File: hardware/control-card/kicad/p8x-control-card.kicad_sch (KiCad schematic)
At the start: 0 parts

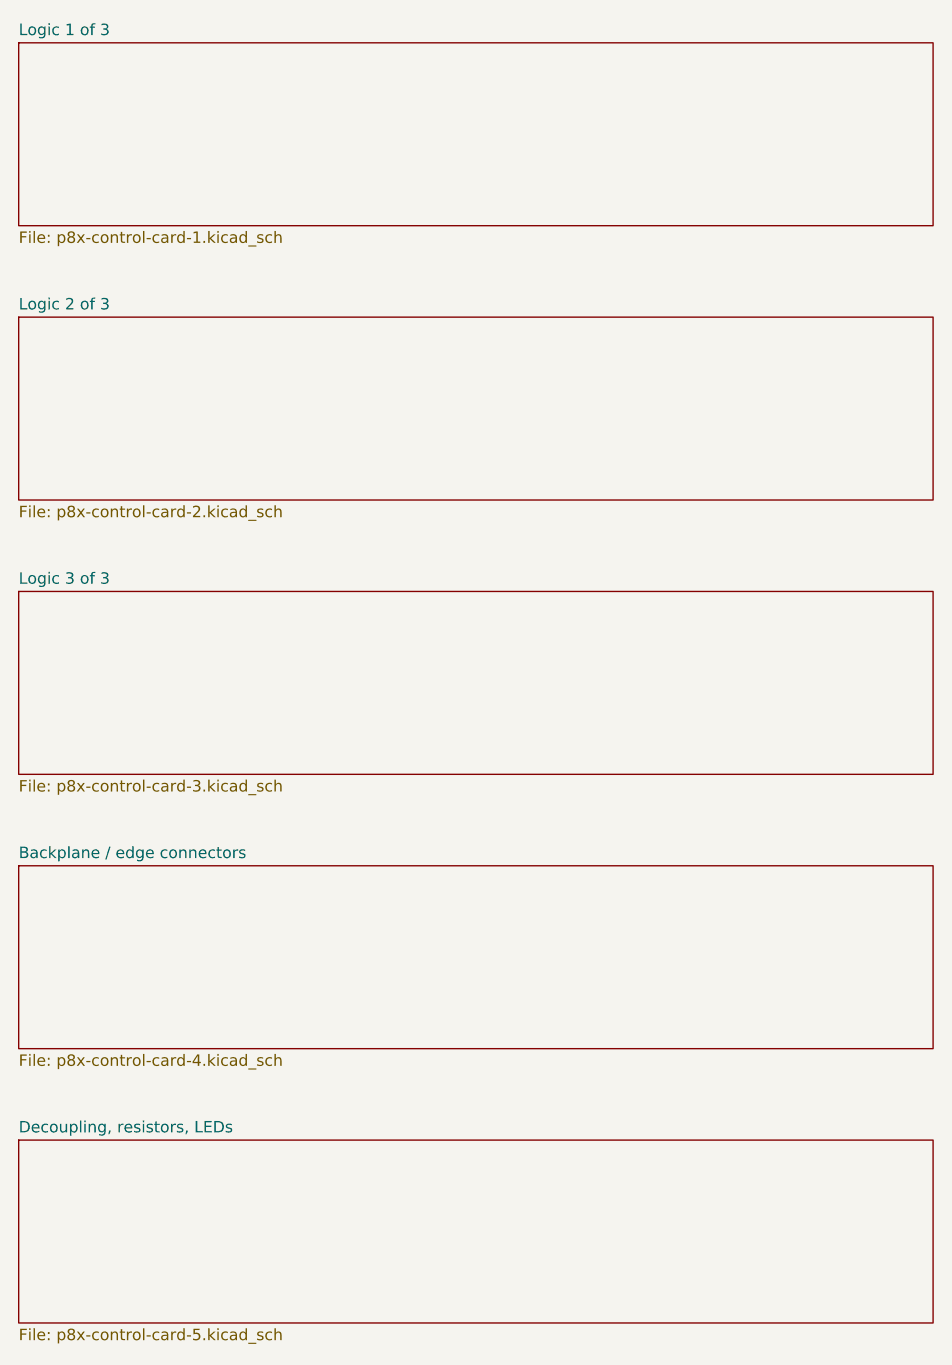
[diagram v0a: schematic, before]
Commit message: feat(sch): draw every P8X card schematic by function
Extend the functional-sheet grouping from the io-card to the control,
regbank, alu, memory, cf, ps2 and bustest cards. functional_sheets now
attaches unnamed glue gates, LEDs, resistors and connectors to the block
they share the most local nets with, so each block lists only its main
parts. A net with two or more pins on a sheet is now wired there even if
it continues elsewhere (its global name label rides on the wire), and
every wire is oriented by drawing side. The regbank gets one pointer per
sheet; the ps2 latches share a sheet with the AVR so the mailbox bus is
drawn. The bustest probe resistors use a straight-order RNISO8DSTR
drawing (the reversed B side forced every wire to cross and the sheet
fell back to labels). build_sch.sh now shows ELK fallbacks and clears old
numbered sheets before a build. All eight netlists match the boards,
ERC 0 errors; the boards change only in footprint link paths.

Co-Authored-By: Claude Opus 5.5 <noreply@anthropic.com>
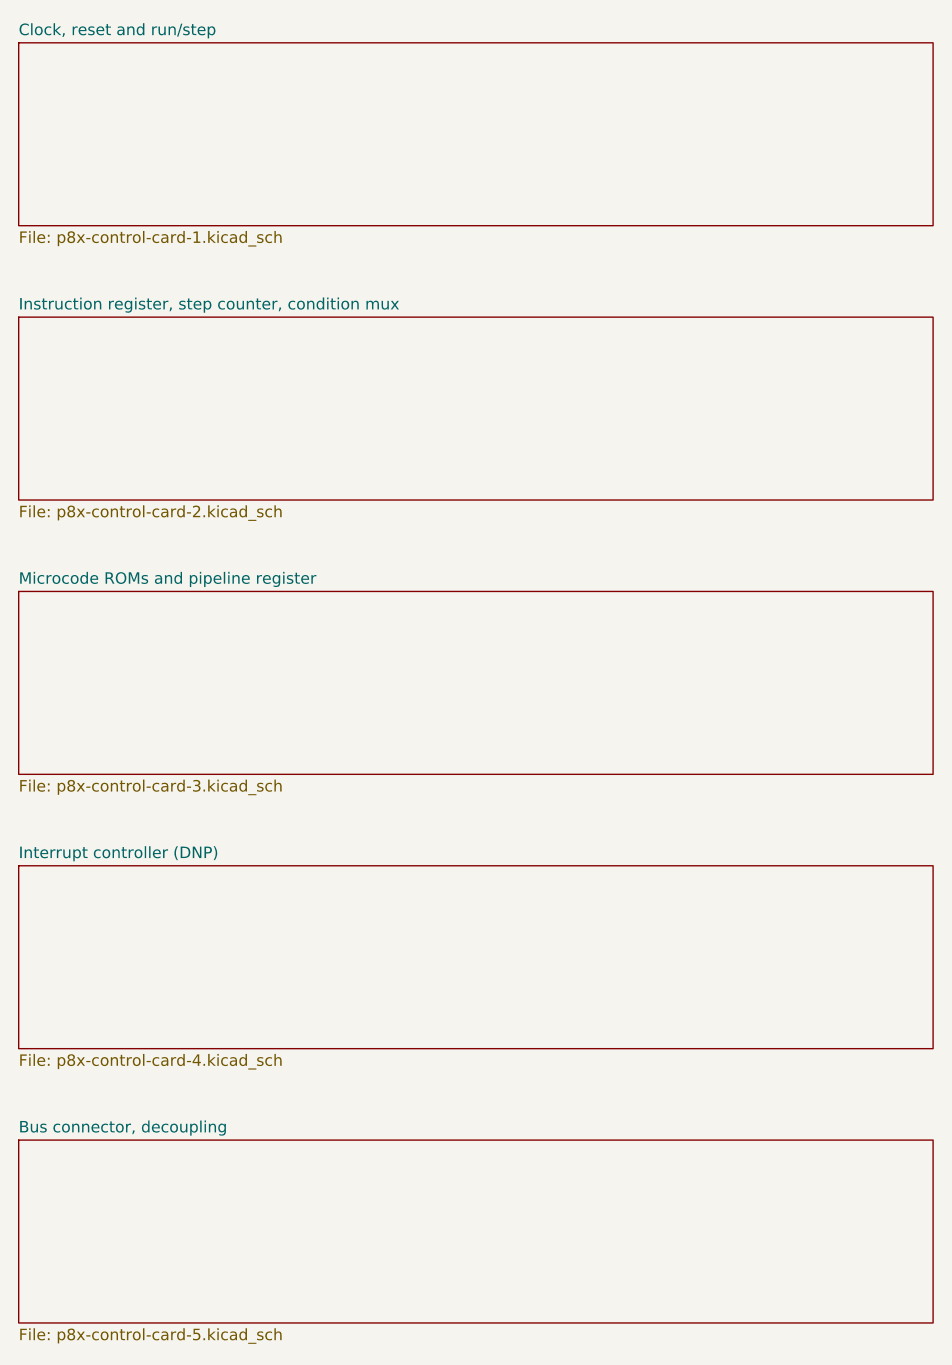
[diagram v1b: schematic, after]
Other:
- sheet Backplane / edge connectors renamed Interrupt controller (DNP)
- sheet Decoupling, resistors, LEDs renamed Bus connector, decoupling
- sheet Logic 1 of 3 renamed Clock, reset and run/step
- sheet Logic 2 of 3 renamed Instruction register, step counter, condition mux
- sheet Logic 3 of 3 renamed Microcode ROMs and pipeline register
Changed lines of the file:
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@@
   (sheet (at 25.40 30.48) (size 101.6 20.32) (fields_autoplaced yes)
     (stroke (width 0.1524) (type solid)) (fill (color 0 0 0 0.0000))
-    (property "Sheetname" "Logic 1 of 3" (at 25.40 29.78 0) (effects (font (size 1.27 1.27)) (justify left bottom)))
+    (property "Sheetname" "Clock, reset and run/step" (at 25.40 29.78 0) (effects (font (size 1.27 1.27)) (justify left bottom)))
     (property "Sheetfile" "p8x-control-card-1.kicad_sch" (at 25.40 51.38 0) (effects (font (size 1.27 1.27)) (justify left top)))
     (instances (project "p8x-control-card" (path "/9cb0414e-6377-55dd-8a6b-04420a5111eb" (page "2"))))
@@
   (sheet (at 25.40 60.96) (size 101.6 20.32) (fields_autoplaced yes)
     (stroke (width 0.1524) (type solid)) (fill (color 0 0 0 0.0000))
-    (property "Sheetname" "Logic 2 of 3" (at 25.40 60.26 0) (effects (font (size 1.27 1.27)) (justify left bottom)))
+    (property "Sheetname" "Instruction register, step counter, condition mux" (at 25.40 60.26 0) (effects (font (size 1.27 1.27)) (justify left bottom)))
     (property "Sheetfile" "p8x-control-card-2.kicad_sch" (at 25.40 81.86 0) (effects (font (size 1.27 1.27)) (justify left top)))
     (instances (project "p8x-control-card" (path "/9cb0414e-6377-55dd-8a6b-04420a5111eb" (page "3"))))
@@
   (sheet (at 25.40 91.44) (size 101.6 20.32) (fields_autoplaced yes)
     (stroke (width 0.1524) (type solid)) (fill (color 0 0 0 0.0000))
-    (property "Sheetname" "Logic 3 of 3" (at 25.40 90.74 0) (effects (font (size 1.27 1.27)) (justify left bottom)))
+    (property "Sheetname" "Microcode ROMs and pipeline register" (at 25.40 90.74 0) (effects (font (size 1.27 1.27)) (justify left bottom)))
     (property "Sheetfile" "p8x-control-card-3.kicad_sch" (at 25.40 112.34 0) (effects (font (size 1.27 1.27)) (justify left top)))
     (instances (project "p8x-control-card" (path "/9cb0414e-6377-55dd-8a6b-04420a5111eb" (page "4"))))
@@
   (sheet (at 25.40 121.92) (size 101.6 20.32) (fields_autoplaced yes)
     (stroke (width 0.1524) (type solid)) (fill (color 0 0 0 0.0000))
-    (property "Sheetname" "Backplane / edge connectors" (at 25.40 121.22 0) (effects (font (size 1.27 1.27)) (justify left bottom)))
+    (property "Sheetname" "Interrupt controller (DNP)" (at 25.40 121.22 0) (effects (font (size 1.27 1.27)) (justify left bottom)))
     (property "Sheetfile" "p8x-control-card-4.kicad_sch" (at 25.40 142.82 0) (effects (font (size 1.27 1.27)) (justify left top)))
     (instances (project "p8x-control-card" (path "/9cb0414e-6377-55dd-8a6b-04420a5111eb" (page "5"))))
@@
   (sheet (at 25.40 152.40) (size 101.6 20.32) (fields_autoplaced yes)
     (stroke (width 0.1524) (type solid)) (fill (color 0 0 0 0.0000))
-    (property "Sheetname" "Decoupling, resistors, LEDs" (at 25.40 151.70 0) (effects (font (size 1.27 1.27)) (justify left bottom)))
+    (property "Sheetname" "Bus connector, decoupling" (at 25.40 151.70 0) (effects (font (size 1.27 1.27)) (justify left bottom)))
     (property "Sheetfile" "p8x-control-card-5.kicad_sch" (at 25.40 173.30 0) (effects (font (size 1.27 1.27)) (justify left top)))
     (instances (project "p8x-control-card" (path "/9cb0414e-6377-55dd-8a6b-04420a5111eb" (page "6"))))
